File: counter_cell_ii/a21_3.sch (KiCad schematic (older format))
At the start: 30 parts, among them U21031 74HC02, U21032 74HC04, U21033 74HC02, U21034 74HC02, U21035 74HC27, U21036 74HC02, U21037 74HC02, U21038 74HC27, U21039 74HC27, U2104 74HC02, U21040 74HC02, U21041 74HC02, U21042 74HC27, U21043 74HC02, U21044 74HC02, U21045 74HC4002, U21046 74HC02, U21047 74HC02, U21048 74HC27, U21049 74HC02, U21050 74HC02, U21051 74HC27, U21052 74HC27, U21053 74HC04, U21054 74HC02, U21055 74HC02, U21056 74HC02, U21057 74HC27, U21058 74HC02, U21059 74HC27

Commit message: Tied in modules 20 and 21
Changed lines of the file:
@@
 	9250 5250 9600 5250
 Wire Wire Line
-	11750 5800 11800 5800
-Text HLabel 11800 5800 2    60   Output ~ 0
-CG15
+	11750 5800 12100 5800
 Text HLabel 10850 5100 2    60   Output ~ 0
 C43A
@@
 	19850 1600 20200 1600
 Wire Wire Line
-	19900 1400 20200 1400
-Text HLabel 19900 1400 0    60   Input ~ 0
-CG15
+	19750 1400 20200 1400
 Text HLabel 21450 1500 2    60   Output ~ 0
 C44A
@@
 	19850 5250 20200 5250
 Wire Wire Line
-	22350 5800 22400 5800
-Text HLabel 22400 5800 2    60   Output ~ 0
-CG16
+	22350 5800 22700 5800
 Text HLabel 21450 5100 2    60   Output ~ 0
 C45A
@@
 $EndComp
 Wire Wire Line
-	20100 8000 20200 8000
-Text HLabel 20100 8000 0    60   Input ~ 0
-CG16
+	19650 8000 20200 8000
 Text HLabel 21450 8100 2    60   Output ~ 0
 C46A
@@
 	1    0    0    -1
 $EndComp
+Text Label 19650 8000 0    60   ~ 0
+CG16
+Text Label 22700 5800 2    60   ~ 0
+CG16
+Text Label 19750 1400 0    60   ~ 0
+CG15
+Text Label 12100 5800 2    60   ~ 0
+CG15
 $EndSCHEMATC

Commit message: Initial conditions for the counter cells
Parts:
- U21033, U21036, U21046, U21049, U21055: Initial (none) -> 1
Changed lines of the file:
@@
 F 2 "" H 6100 1600 60  0000 C CNN
 F 3 "" H 6100 1600 60  0000 C CNN
+F 4 "1" H 6350 1600 60  0000 C CIN "Initial"
 	1    6100 1600
 	1    0    0    -1
@@
 F 2 "" H 6100 5250 60  0000 C CNN
 F 3 "" H 6100 5250 60  0000 C CNN
+F 4 "1" H 6350 5250 60  0000 C CIN "Initial"
 	2    6100 5250
 	1    0    0    -1
@@
 F 2 "" H 16700 1600 60  0000 C CNN
 F 3 "" H 16700 1600 60  0000 C CNN
+F 4 "1" H 16950 1600 60  0000 C CIN "Initial"
 	2    16700 1600
 	1    0    0    -1
@@
 F 2 "" H 16700 5250 60  0000 C CNN
 F 3 "" H 16700 5250 60  0000 C CNN
+F 4 "1" H 16950 5250 60  0000 C CIN "Initial"
 	3    16700 5250
 	1    0    0    -1
@@
 F 2 "" H 16450 9000 60  0000 C CNN
 F 3 "" H 16450 9000 60  0000 C CNN
+F 4 "1" H 16700 9000 60  0000 C CIN "Initial"
 	3    16450 9000
 	1    0    0    -1

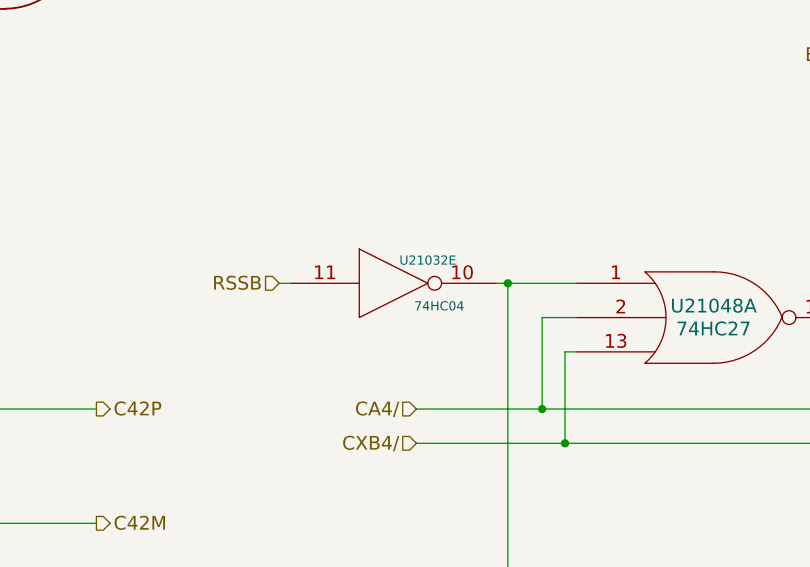
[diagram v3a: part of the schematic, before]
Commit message: Lots of initial conditions, some missed gates, and some wiring fixes
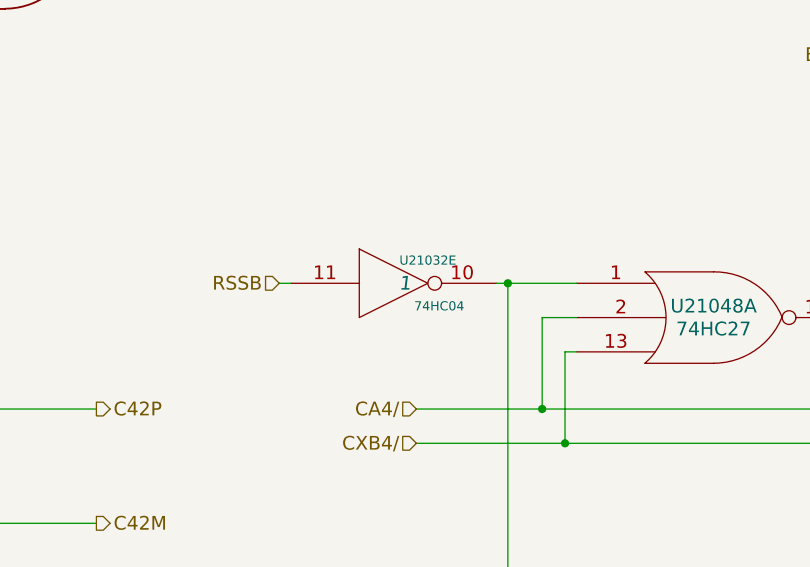
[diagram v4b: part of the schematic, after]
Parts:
- U21032: Initial (none) -> 1
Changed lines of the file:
@@
 F 2 "" H 11900 2900 60  0000 C CNN
 F 3 "" H 11900 2900 60  0000 C CNN
+F 4 "1" H 11950 2900 60  0000 C CIN "Initial"
 	5    11900 2900
 	1    0    0    -1

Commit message: Fixed not->1-input nor in the rest of the modules.
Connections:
- wire segments 436 -> 454
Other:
- moved on the sheet: U21031A, U21031B, U21031C, U21031D, U21032A, U21032B, U21032C, U21032D, U21032E, U21032F, U21033A, U21033B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

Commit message: Power net updates for Counter Cell I+II and Inout V
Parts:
- renumbered U2104 to U21029, U21031 to U21030, U21032 to U21031, U21033 to U21032, U21034 to U21033, U21035 to U21034, U21036 to U21035, U21037 to U21036, U21038 to U21037, U21039 to U21038, U21040 to U21039, U21041 to U21040, U21042 to U21041, U21043 to U21042, U21044 to U21043, U21045 to U21044, U21046 to U21045, U21047 to U21046, U21048 to U21047, U21049 to U21048, U21050 to U21049, U21051 to U21050, U21052 to U21051, U21053 to U21052, U21054 to U21053, U21055 to U21054, U21058 to U21054, U21056 to U21055, U21058 to U21055, U21057 to U21056, U21059 to U21057
